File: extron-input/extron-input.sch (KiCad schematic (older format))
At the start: 20 parts, among them J1 SCART-F, J10 Conn_01x01, J11 Conn_01x01, J2 RED, J3 GREEN, J4 BLUE, J5 SYNC, J6 PHOENIX, J7 SENSE, J8 Conn_01x01, J9 Conn_01x01, SW1 SW_DPDT_x2, U1 LM1881

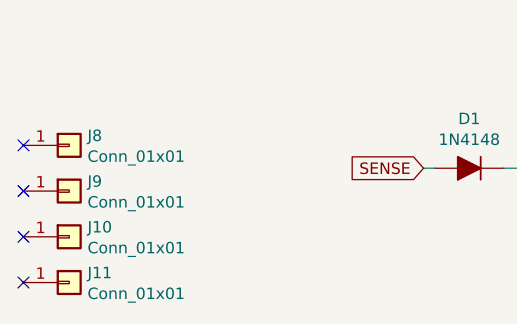
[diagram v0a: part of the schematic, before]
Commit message: WIP on input board v3
New features:
  Longer boards that support top/bottom placement, allowing closer
  placement for extron 300 ADSP models, and allowing thicker FR4 again

  Will have new RCA placements to support both older and newer extron
  BNC spacings
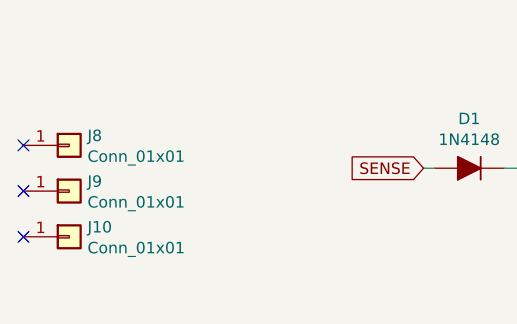
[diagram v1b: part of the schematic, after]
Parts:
- removed J11: Conn_01x01, MountingHole:MountingHole_3.2mm_M3, symbol Connector_Generic:Conn_01x01
- J6: footprint Connector_JST:JST_XH_S03B-XH-A_1x03_P2.50mm_Horizontal -> Connector_JST:JST_XH_S3B-XH-A-1_1x03_P2.50mm_Horizontal
- J7: footprint Connector_JST:JST_XH_S02B-XH-A_1x02_P2.50mm_Horizontal -> Connector_JST:JST_XH_S2B-XH-A_1x02_P2.50mm_Horizontal
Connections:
- no-connect marks 11 -> 10
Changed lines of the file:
@@
 F 0 "J6" H 4756 5028 50  0000 C CNN
 F 1 "PHOENIX" H 4756 4937 50  0000 C CNN
-F 2 "Connector_JST:JST_XH_S03B-XH-A_1x03_P2.50mm_Horizontal" H 4650 4750 50  0001 C CNN
+F 2 "Connector_JST:JST_XH_S3B-XH-A-1_1x03_P2.50mm_Horizontal" H 4650 4750 50  0001 C CNN
 F 3 "~" H 4650 4750 50  0001 C CNN
 F 4 "https://lcsc.com/product-detail/XH-Connectors_JST_S3B-XH-A-LF-SN_XHsocket-1-3P-Curved-needle-pitch2-5mm_C157928.html" H 4650 4750 50  0001 C CNN "Vendor"
@@
 F 0 "J7" H 5900 5600 50  0000 R CNN
 F 1 "SENSE" H 5700 5800 50  0000 R CNN
-F 2 "Connector_JST:JST_XH_S02B-XH-A_1x02_P2.50mm_Horizontal" H 5750 5800 50  0001 C CNN
+F 2 "Connector_JST:JST_XH_S2B-XH-A_1x02_P2.50mm_Horizontal" H 5750 5800 50  0001 C CNN
 F 3 "~" H 5750 5800 50  0001 C CNN
 F 4 "https://lcsc.com/product-detail/XH-Connectors_JST_S2B-XH-A-LF-SN_XHsocket-1-2P-Curved-needle-pitch2-5mm_C157931.html" H 5750 5800 50  0001 C CNN "Vendor"
@@
 NoConn ~ 2400 5800
 NoConn ~ 2400 6000
-NoConn ~ 2400 6200
 $Comp
 L Connector_Generic:Conn_01x01 J8
@@
 	1    0    0    -1
 $EndComp
-$Comp
-L Connector_Generic:Conn_01x01 J11
-U 1 1 5C7607B9
-P 2600 6200
-F 0 "J11" H 2680 6242 50  0000 L CNN
-F 1 "Conn_01x01" H 2680 6151 50  0000 L CNN
-F 2 "MountingHole:MountingHole_3.2mm_M3" H 2600 6200 50  0001 C CNN
-F 3 "~" H 2600 6200 50  0001 C CNN
-	1    2600 6200
-	1    0    0    -1
-$EndComp
